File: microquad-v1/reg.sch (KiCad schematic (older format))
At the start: 3 parts

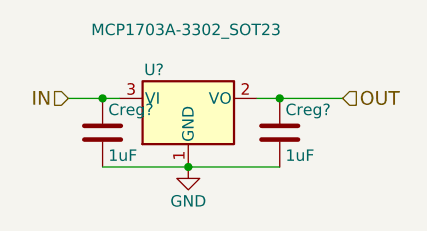
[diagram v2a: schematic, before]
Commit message: Fixed DRC errors (the ladybug is now happy)
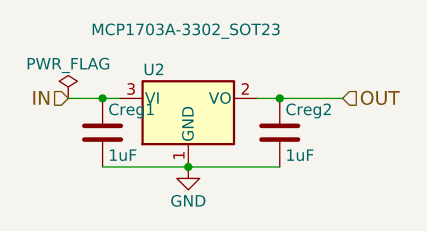
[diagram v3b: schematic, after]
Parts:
- gave numbers to parts that had none: 3
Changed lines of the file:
@@
 $Descr A4 11693 8268
 encoding utf-8
-Sheet 2 8
+Sheet 2 9
 Title ""
 Date ""
@@
 $EndDescr
 $Comp
-L MCP1703A-3302_SOT23 U?
+L MCP1703A-3302_SOT23 U2
 U 1 1 59F29DB0
 P 4250 3300
-F 0 "U?" H 4100 3425 50  0000 C CNN
+F 0 "U2" H 4100 3425 50  0000 C CNN
 F 1 "MCP1703A-3302_SOT23" H 3825 3600 50  0000 L CNN
 F 2 "TO_SOT_Packages_SMD:SOT-23" H 4250 3500 50  0001 C CNN
@@
 $EndComp
 $Comp
-L GND #PWR04
+L GND #PWR014
 U 1 1 59F29DBE
 P 4250 3600
-F 0 "#PWR04" H 4250 3350 50  0001 C CNN
+F 0 "#PWR014" H 4250 3350 50  0001 C CNN
 F 1 "GND" H 4250 3450 50  0000 C CNN
 F 2 "" H 4250 3600 50  0001 C CNN
@@
 $EndComp
 $Comp
-L C Creg?
+L C Creg2
 U 1 1 59F29DCA
 P 4650 3450
-F 0 "Creg?" H 4675 3550 50  0000 L CNN
+F 0 "Creg2" H 4675 3550 50  0000 L CNN
 F 1 "1uF" H 4675 3350 50  0000 L CNN
 F 2 "Capacitors_SMD:C_0603" H 4688 3300 50  0001 C CNN
@@
 $EndComp
 $Comp
-L C Creg?
+L C Creg1
 U 1 1 59F29DD1
 P 3875 3450
-F 0 "Creg?" H 3900 3550 50  0000 L CNN
+F 0 "Creg1" H 3900 3550 50  0000 L CNN
 F 1 "1uF" H 3900 3350 50  0000 L CNN
 F 2 "Capacitors_SMD:C_0603" H 3913 3300 50  0001 C CNN
@@
 Text HLabel 3725 3300 0    60   Input ~ 0
 IN
+$Comp
+L PWR_FLAG #FLG015
+U 1 1 59FC3CDA
+P 3725 3300
+F 0 "#FLG015" H 3725 3375 50  0001 C CNN
+F 1 "PWR_FLAG" H 3725 3450 50  0000 C CNN
+F 2 "" H 3725 3300 50  0001 C CNN
+F 3 "" H 3725 3300 50  0001 C CNN
+	1    3725 3300
+	1    0    0    -1
+$EndComp
 $EndSCHEMATC
